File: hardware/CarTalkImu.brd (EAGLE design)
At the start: 38.1 x 40.6 mm, 11 parts, among them J4 1X10, J5 1X10, U3 MPU9250, U4 NEO-M8

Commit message: Finalized Rev 1A schematic and layout.
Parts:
- added C1, C3, C4, C5, C6, C7: 100n, CarTalkImu:C0603
- added C10, C8: 10u, CarTalkImu:C0603
- added C11, C9: 1u, CarTalkImu:C0603
- added C2: 10n, CarTalkImu:C0603
- added R1, R2, R3, R4, R5: 10k, CarTalkImu:R0603
- added R10, R11, R6, R7, R8, R9: 220, CarTalkImu:R0603
- added U1: LPS22HB, CarTalkImu:HLGA-10L
- added X1: (no value), CarTalkImu:ESP-12
- U4: value NEO-M8 -> CAM-M8; device CarTalkImu:NEO-M8 -> CarTalkImu:CAM-M8
- moved U$5 40.4 mm to (28.6, 6.99)
- moved U3 8.47 mm to (22.2, 29.2), flipped to the bottom, turned to 180 degrees
- moved U4 8.26 mm to (20.3, 8.26), flipped to the top, turned to 180 degrees
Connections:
- removed net XB_MULT2: J5.5
- removed net XB_MULT3: J5.9
- removed net XB_MULT5: J4.8
- removed net XB_MULT6: J5.10
- new net N$10: R6.2, U4.26
- new net N$11: R7.2, U4.25
- new net N$12: R8.2, U4.6
- new net N$13: R9.2, U4.3
- new net N$14: U4.16, U4.17
- new net N$15: R10.2, X1.16
- new net N$16: R11.2, X1.15
- new net N$4: C1.1, U3.10
- new net N$6: R1.1, X1.12
- new net N$7: R2.1, X1.11
- new net N$8: R3.1, X1.10
- new net N$9: R4.1, X1.3
- new net XB_MULT2/PRESS_CS: J5.5, U1.6
- new net XB_MULT3/TMPLSE: J5.9, U4.29
- new net XB_MULT5/MPU_CS: J4.8, U3.22
- new net XB_MULT6/GPS_CS: J5.10, R9.1
- net +3V3: now also C10.1, C11.1, C2.1, C3.1, C4.1, C5.1, C7.1, C8.1, C9.1, R1.2, R2.2, R4.2, R5.2, U1.1, U1.10, U3.1, U3.13, U3.8, U4.1, U4.8, U4.9, X1.8
- net DGND: now also C1.2, C10.2, C11.2, C2.2, C3.2, C4.2, C5.2, C6.2, C7.2, C8.2, C9.2, R3.2, U1.3, U1.8, U1.9, U3.11, U3.18, U3.20, U4.10, U4.11, U4.12, U4.13, U4.14, U4.15, U4.18, U4.19, U4.20, U4.21, U4.22, U4.27, U4.31, U4.4, U4.5, X1.9
- net SPI0_CLK: now also R8.1, U1.2, U3.23
- net SPI0_MISO: now also R7.1, U1.5, U3.9
- net SPI0_MOSI: now also R6.1, U1.4, U3.24
- net XB_NRST: now also C6.1, R5.1, U4.23, X1.1
- net XB_UART_RX: now also R10.1
- net XB_UART_TX: now also R11.1
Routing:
- net +3V3: track 0.00 -> 134.7 mm, vias 0 -> 9
- net XB_NRST: track 0.00 -> 59.7 mm, vias 0 -> 2
- net SPI0_CLK: track 0.00 -> 38.8 mm, vias 0 -> 2
- net SPI0_MOSI: track 0.00 -> 37.1 mm, vias 0 -> 3
- net SPI0_MISO: track 0.00 -> 34.6 mm, vias 0 -> 3
- net XB_UART_RX: track 0.00 -> 21.4 mm, vias 0 -> 1
- net XB_MULT5/MPU_CS: track 0.00 -> 19.9 mm, vias 0 -> 3
- net XB_MULT3/TMPLSE: track 0.00 -> 14.3 mm, vias 0 -> 1
- net XB_UART_TX: track 0.00 -> 13.9 mm, vias 0 -> 1
- net XB_MULT2/PRESS_CS: track 0.00 -> 8.97 mm
- net N$6: track 0.00 -> 7.32 mm
- net N$8: track 0.00 -> 7.24 mm
- net N$16: track 0.00 -> 7.21 mm
- net N$15: track 0.00 -> 7.17 mm
- net N$7: track 0.00 -> 7.10 mm
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- added copper zone on layer 1, net DGND
- added copper zone on layer 15, net DGND
- added copper zone on layer 16, net DGND
- added copper zone on layer 2, net DGND

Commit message: Re-finalized design and layout.
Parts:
- X1: value (none) -> ESP-12
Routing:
- net +3V3: track 134.7 -> 135.4 mm
- net DGND: vias 0 -> 87
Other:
- outline, holes or cut-outs redrawn

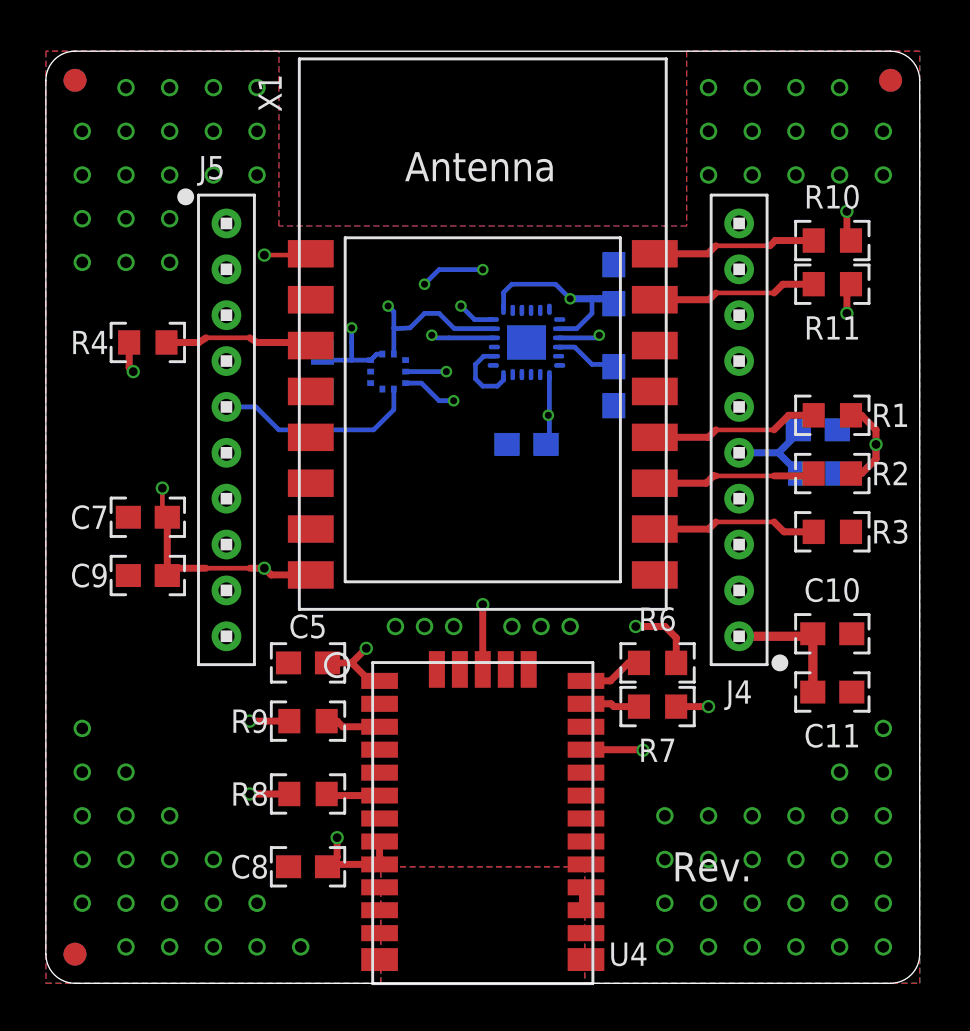
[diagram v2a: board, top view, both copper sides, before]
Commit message: Simplified board layout a bit.
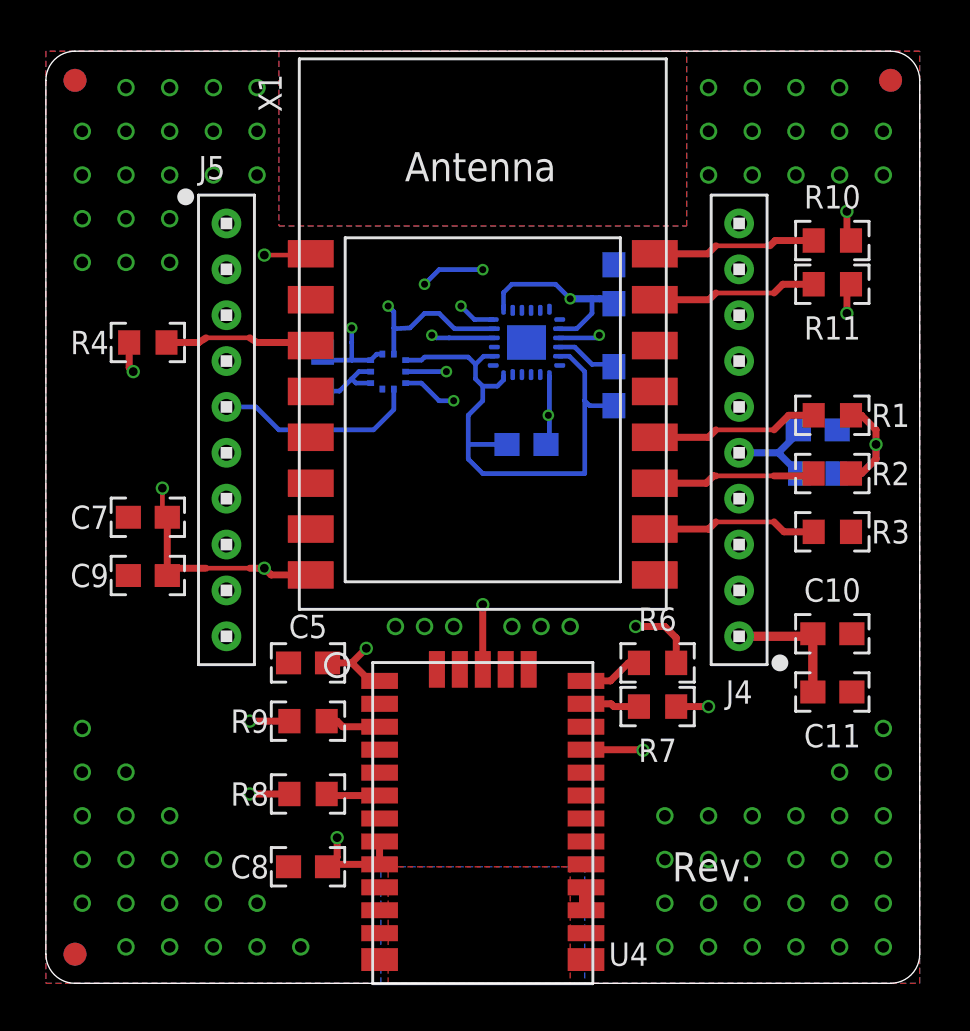
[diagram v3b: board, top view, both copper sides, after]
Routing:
- net DGND: track 3.25 -> 27.5 mm
- added copper zone on layer 1, net N$1
- added copper zone on layer 1, net N$17
- added copper zone on layer 15, net N$17
- added copper zone on layer 16, net N$17
- added copper zone on layer 2, net N$17
- added copper zone on layer 2, net N$2
- added copper zone on layer 15, net N$3
- added copper zone on layer 16, net N$5
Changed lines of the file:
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@@
 <layer number="17" name="Pads" color="2" fill="1" visible="yes" active="yes"/>
 <layer number="18" name="Vias" color="2" fill="1" visible="yes" active="yes"/>
-<layer number="19" name="Unrouted" color="6" fill="1" visible="yes" active="yes"/>
+<layer number="19" name="Unrouted" color="6" fill="1" visible="no" active="yes"/>
 <layer number="20" name="Dimension" color="15" fill="1" visible="yes" active="yes"/>
-<layer number="21" name="tPlace" color="7" fill="1" visible="yes" active="yes"/>
-<layer number="22" name="bPlace" color="7" fill="1" visible="yes" active="yes"/>
-<layer number="23" name="tOrigins" color="15" fill="1" visible="yes" active="yes"/>
-<layer number="24" name="bOrigins" color="15" fill="1" visible="yes" active="yes"/>
-<layer number="25" name="tNames" color="7" fill="1" visible="yes" active="yes"/>
-<layer number="26" name="bNames" color="7" fill="1" visible="yes" active="yes"/>
-<layer number="27" name="tValues" color="7" fill="1" visible="yes" active="yes"/>
-<layer number="28" name="bValues" color="7" fill="1" visible="yes" active="yes"/>
+<layer number="21" name="tPlace" color="7" fill="1" visible="no" active="yes"/>
+<layer number="22" name="bPlace" color="7" fill="1" visible="no" active="yes"/>
+<layer number="23" name="tOrigins" color="15" fill="1" visible="no" active="yes"/>
+<layer number="24" name="bOrigins" color="15" fill="1" visible="no" active="yes"/>
+<layer number="25" name="tNames" color="7" fill="1" visible="no" active="yes"/>
+<layer number="26" name="bNames" color="7" fill="1" visible="no" active="yes"/>
+<layer number="27" name="tValues" color="7" fill="1" visible="no" active="yes"/>
+<layer number="28" name="bValues" color="7" fill="1" visible="no" active="yes"/>
 <layer number="29" name="tStop" color="7" fill="3" visible="no" active="yes"/>
 <layer number="30" name="bStop" color="7" fill="6" visible="no" active="yes"/>
@@
 <layer number="37" name="tTest" color="7" fill="1" visible="no" active="yes"/>
 <layer number="38" name="bTest" color="7" fill="1" visible="no" active="yes"/>
-<layer number="39" name="tKeepout" color="4" fill="11" visible="yes" active="yes"/>
-<layer number="40" name="bKeepout" color="1" fill="11" visible="yes" active="yes"/>
-<layer number="41" name="tRestrict" color="4" fill="10" visible="yes" active="yes"/>
-<layer number="42" name="bRestrict" color="1" fill="10" visible="yes" active="yes"/>
-<layer number="43" name="vRestrict" color="2" fill="10" visible="yes" active="yes"/>
-<layer number="44" name="Drills" color="7" fill="1" visible="yes" active="yes"/>
+<layer number="39" name="tKeepout" color="4" fill="11" visible="no" active="yes"/>
+<layer number="40" name="bKeepout" color="1" fill="11" visible="no" active="yes"/>
+<layer number="41" name="tRestrict" color="4" fill="10" visible="no" active="yes"/>
+<layer number="42" name="bRestrict" color="1" fill="10" visible="no" active="yes"/>
+<layer number="43" name="vRestrict" color="2" fill="10" visible="no" active="yes"/>
+<layer number="44" name="Drills" color="7" fill="1" visible="no" active="yes"/>
 <layer number="45" name="Holes" color="7" fill="1" visible="yes" active="yes"/>
 <layer number="46" name="Milling" color="3" fill="1" visible="no" active="yes"/>
@@
 <contactref element="C11" pad="2"/>
 <contactref element="C10" pad="2"/>
-<polygon width="0.254" layer="1">
+<polygon width="0.254" layer="1" isolate="0.254">
 <vertex x="1.27" y="1.27"/>
-<vertex x="15.875" y="1.27"/>
-<vertex x="15.875" y="6.35"/>
-<vertex x="24.765" y="6.35"/>
-<vertex x="24.765" y="1.27"/>
 <vertex x="39.37" y="1.27"/>
 <vertex x="39.37" y="41.91"/>
-<vertex x="29.21" y="41.91"/>
-<vertex x="29.21" y="34.29"/>
-<vertex x="11.43" y="34.29"/>
-<vertex x="11.43" y="41.91"/>
 <vertex x="1.27" y="41.91"/>
 </polygon>
-<polygon width="0.254" layer="15">
+<polygon width="0.254" layer="15" isolate="0.254">
 <vertex x="1.27" y="1.27"/>
-<vertex x="15.875" y="1.27"/>
-<vertex x="15.875" y="6.35"/>
-<vertex x="24.765" y="6.35"/>
-<vertex x="24.765" y="1.27"/>
 <vertex x="39.37" y="1.27"/>
 <vertex x="39.37" y="41.91"/>
-<vertex x="29.21" y="41.91"/>
-<vertex x="29.21" y="34.29"/>
-<vertex x="11.43" y="34.29"/>
-<vertex x="11.43" y="41.91"/>
 <vertex x="1.27" y="41.91"/>
 </polygon>
-<polygon width="0.2032" layer="16">
+<polygon width="0.254" layer="16" isolate="0.254">
 <vertex x="1.27" y="1.27"/>
-<vertex x="15.875" y="1.27"/>
-<vertex x="15.875" y="6.35"/>
-<vertex x="24.765" y="6.35"/>
-<vertex x="24.765" y="1.27"/>
 <vertex x="39.37" y="1.27"/>
 <vertex x="39.37" y="41.91"/>
-<vertex x="29.21" y="41.91"/>
-<vertex x="29.21" y="34.29"/>
-<vertex x="11.43" y="34.29"/>
-<vertex x="11.43" y="41.91"/>
 <vertex x="1.27" y="41.91"/>
 </polygon>
@@
 <wire x1="20.0025" y1="27.6225" x2="20.0025" y2="28.2575" width="0.2032" layer="16"/>
 <contactref element="U3" pad="11"/>
-<polygon width="0.2032" layer="2">
+<polygon width="0.254" layer="2" isolate="0.254">
 <vertex x="1.27" y="1.27"/>
-<vertex x="15.875" y="1.27"/>
-<vertex x="15.875" y="6.35"/>
-<vertex x="24.765" y="6.35"/>
-<vertex x="24.765" y="1.27"/>
 <vertex x="39.37" y="1.27"/>
 <vertex x="39.37" y="41.91"/>
-<vertex x="29.21" y="41.91"/>
-<vertex x="29.21" y="34.29"/>
-<vertex x="11.43" y="34.29"/>
-<vertex x="11.43" y="41.91"/>
 <vertex x="1.27" y="41.91"/>
 </polygon>
@@
 <via x="24.13" y="16.8275" extent="1-16" drill="0.508"/>
 <via x="16.51" y="16.8275" extent="1-16" drill="0.508"/>
+<wire x1="23.625" y1="28.61" x2="24.095" y2="28.61" width="0.2032" layer="16"/>
+<wire x1="24.095" y1="28.61" x2="24.765" y2="27.94" width="0.2032" layer="16"/>
+<wire x1="24.765" y1="27.94" x2="24.765" y2="26.67" width="0.2032" layer="16"/>
+<wire x1="24.765" y1="26.67" x2="24.765" y2="23.495" width="0.2032" layer="16"/>
+<wire x1="24.765" y1="23.495" x2="20.32" y2="23.495" width="0.2032" layer="16"/>
+<wire x1="20.32" y1="23.495" x2="19.685" y2="24.13" width="0.2032" layer="16"/>
+<wire x1="19.685" y1="24.13" x2="19.685" y2="24.765" width="0.2032" layer="16"/>
+<wire x1="19.685" y1="24.765" x2="19.685" y2="26.035" width="0.2032" layer="16"/>
+<wire x1="21.375" y1="24.765" x2="19.685" y2="24.765" width="0.2032" layer="16"/>
+<wire x1="20.32" y1="27.305" x2="20.32" y2="26.67" width="0.2032" layer="16"/>
+<wire x1="20.32" y1="26.67" x2="19.685" y2="26.035" width="0.2032" layer="16"/>
+<wire x1="26.035" y1="26.455" x2="24.98" y2="26.455" width="0.2032" layer="16"/>
+<wire x1="24.98" y1="26.455" x2="24.765" y2="26.67" width="0.2032" layer="16"/>
+<wire x1="16.955" y1="28.44" x2="17.645" y2="28.44" width="0.2032" layer="16"/>
+<wire x1="17.645" y1="28.44" x2="17.78" y2="28.575" width="0.2032" layer="16"/>
+<wire x1="17.78" y1="28.575" x2="19.685" y2="28.575" width="0.2032" layer="16"/>
+<wire x1="19.685" y1="28.575" x2="20.0025" y2="28.2575" width="0.2032" layer="16"/>
+<wire x1="15.43" y1="27.44" x2="14.7875" y2="27.44" width="0.2032" layer="16"/>
+<wire x1="14.7875" y1="27.44" x2="14.605" y2="27.6225" width="0.2032" layer="16"/>
+<wire x1="15.43" y1="27.94" x2="14.9225" y2="27.94" width="0.2032" layer="16"/>
+<wire x1="14.9225" y1="27.94" x2="14.605" y2="27.6225" width="0.2032" layer="16"/>
+<wire x1="13.335" y1="27.09" x2="14.0725" y2="27.09" width="0.2032" layer="16"/>
+<wire x1="14.0725" y1="27.09" x2="14.605" y2="27.6225" width="0.2032" layer="16"/>
 </signal>
 <signal name="XB_MULT3/TMPLSE">
@@
 <wire x1="9.2075" y1="16.3365" x2="9.144" y2="16.4" width="0.3048" layer="2"/>
 </signal>
+<signal name="N$1">
+<polygon width="0.254" layer="1" pour="cutout">
+<vertex x="11.43" y="41.91"/>
+<vertex x="11.43" y="34.29"/>
+<vertex x="29.21" y="34.29"/>
+<vertex x="29.21" y="41.91"/>
+</polygon>
+</signal>
+<signal name="N$2">
+<polygon width="0.254" layer="2" pour="cutout">
+<vertex x="11.43" y="41.91"/>
+<vertex x="11.43" y="34.29"/>
+<vertex x="29.21" y="34.29"/>
+<vertex x="29.21" y="41.91"/>
+</polygon>
+</signal>
+<signal name="N$3">
+<polygon width="0.254" layer="15" pour="cutout">
+<vertex x="11.43" y="41.91"/>
+<vertex x="11.43" y="34.29"/>
+<vertex x="29.21" y="34.29"/>
+<vertex x="29.21" y="41.91"/>
+</polygon>
+</signal>
+<signal name="N$5">
+<polygon width="0.254" layer="16" pour="cutout">
+<vertex x="11.43" y="41.91"/>
+<vertex x="11.43" y="34.29"/>
+<vertex x="29.21" y="34.29"/>
+<vertex x="29.21" y="41.91"/>
+</polygon>
+</signal>
+<signal name="N$17">
+<polygon width="0.254" layer="1" pour="cutout">
+<vertex x="16.1925" y="1.27"/>
+<vertex x="16.1925" y="6.35"/>
+<vertex x="24.13" y="6.35"/>
+<vertex x="24.13" y="1.27"/>
+</polygon>
+<polygon width="0.254" layer="16" pour="cutout">
+<vertex x="15.875" y="1.27"/>
+<vertex x="15.875" y="6.35"/>
+<vertex x="24.765" y="6.35"/>
+<vertex x="24.765" y="1.27"/>
+</polygon>
+<polygon width="0.254" layer="15" pour="cutout">
+<vertex x="15.875" y="1.27"/>
+<vertex x="15.875" y="6.35"/>
+<vertex x="24.765" y="6.35"/>
+<vertex x="24.765" y="1.27"/>
+</polygon>
+<polygon width="0.254" layer="2" pour="cutout">
+<vertex x="15.875" y="1.27"/>
+<vertex x="15.875" y="6.35"/>
+<vertex x="24.765" y="6.35"/>
+<vertex x="24.765" y="1.27"/>
+</polygon>
+</signal>
 </signals>

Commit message: Replaced LPS22 part with BME680 part. Upated board layout.
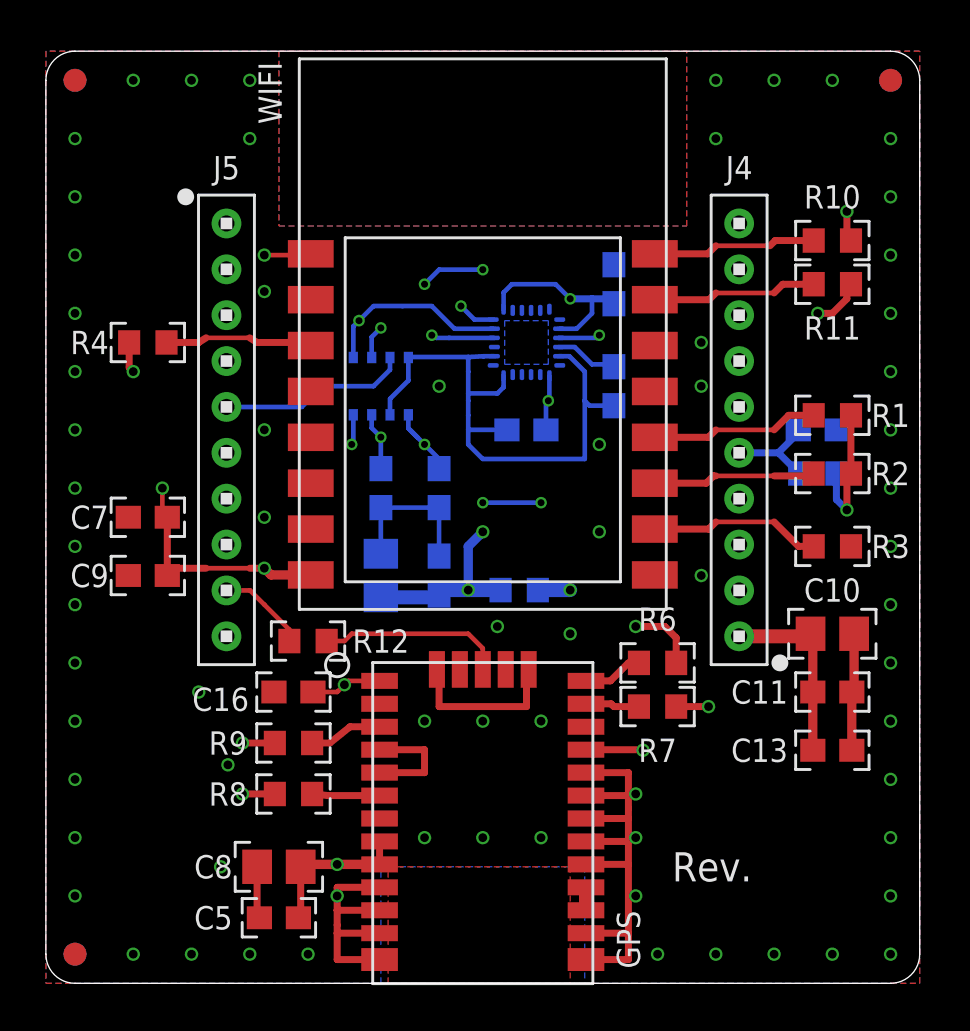
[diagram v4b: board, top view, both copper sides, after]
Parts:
- removed U1: LPS22HB, CarTalkImu:HLGA-10L
- removed U3: MPU9250, CarTalkImu:QFN24
- added C12, C13, C14, C16: 100n, CarTalkImu:C0603
- added C15: 10u, CarTalkImu:C0805
- added FB1: 10, CarTalkImu:R0603
- added IMU: MPU9250, CarTalkImu:QFN24-NP
- added R12: 220, CarTalkImu:R0603
- added TPH: BME680, CarTalkImu:BME-DFN8
- C10, C8: device CarTalkImu:C0603 -> CarTalkImu:C0805
- C4: value 100n -> 10n
- moved C5 11.2 mm to (11.4, 4.13)
- moved C4 5.68 mm to (15.9, 22.9)
- moved C8 1.27 mm to (11.4, 6.35)
- moved R9 1.14 mm to (12.1, 11.7)
- moved R8 0.63 mm to (12.1, 9.53)
- moved C3 0.63 mm to (22.2, 25.4)
- moved R3 0.63 mm to (35.6, 20.3)
- renumbered U4 to GPS, X1 to WIFI
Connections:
- removed net XB_MULT2/PRESS_CS: J5.5, U1.6
- new net +3V3A: C12.1, C14.1, C15.1, C3.1, C5.1, C8.1, FB1.1, GPS.8, GPS.9, IMU.13, TPH.8
- new net N$18: GPS.29, R12.2
- new net XB_MULT2/TPH_CS: J5.5, TPH.2
- net +3V3: now also C13.1, C16.1, FB1.2, IMU.1, IMU.8, TPH.6; no longer C3.1, C5.1, C8.1, GPS.8, GPS.9, U1.1, U1.10, U3.1, U3.13, U3.8
- net DGND: now also C12.2, C13.2, C14.2, C15.2, C16.2, IMU.11, IMU.18, IMU.20, TPH.1, TPH.7; no longer U1.3, U1.8, U1.9, U3.11, U3.18, U3.20
- net N$4: now also IMU.10; no longer U3.10
- net SPI0_CLK: now also IMU.23, TPH.4; no longer U1.2, U3.23
- net SPI0_MISO: now also IMU.9, TPH.5; no longer U1.5, U3.9
- net SPI0_MOSI: now also IMU.24, TPH.3; no longer U1.4, U3.24
- net XB_MULT3/TMPLSE: now also R12.1; no longer GPS.29
- net XB_MULT5/MPU_CS: now also IMU.22; no longer U3.22
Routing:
- net DGND: track 27.5 -> 84.1 mm, vias 87 -> 69
- net +3V3A: track 0.00 -> 47.9 mm, vias 0 -> 5
- net +3V3: track 135.4 -> 105.2 mm, vias 9 -> 8
- net XB_MULT3/TMPLSE: track 14.3 -> 3.95 mm, vias 1 -> 0
- net SPI0_MISO: track 34.6 -> 43.8 mm, vias 3 -> 5
- net XB_MULT2/PRESS_CS: track 8.97 -> 0.00 mm
- net XB_MULT2/TPH_CS: track 0.00 -> 8.34 mm
- net N$18: track 0.00 -> 8.12 mm
- net SPI0_MOSI: track 37.1 -> 38.9 mm
- net XB_UART_RX: track 21.4 -> 20.3 mm
- net N$13: track 2.41 -> 3.19 mm
- net SPI0_CLK: track 38.8 -> 38.1 mm
- net N$12: track 2.34 -> 2.95 mm
- net XB_MULT6/GPS_CS: track 5.85 -> 6.35 mm
- added copper zone on layer 15, net N$19
- added copper zone on layer 16, net N$19
- added copper zone on layer 2, net N$19
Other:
- board text added: "PCB Layer Stack-up: L1: top components + ground plane L2: signals + RF traces L3: ground + power planes L4: ground plane, short traces"

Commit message: Fixed minor layout/DFM issues
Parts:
- renumbered IMU to MPU
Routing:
- net +3V3: track 105.2 -> 102.0 mm
